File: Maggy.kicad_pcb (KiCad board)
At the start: 2 copper layers, 160 x 100 mm, 75 parts, among them CN1 0430450800, CN2 430451000, J1 XY308-2.54-2P, J2 XY308-2.54-2P, J3 XY308-2.54-2P, J4 XY308-2.54-2P, U1 CH224K, U10 INA214AIDCKR, U11 Socket for Teensy 4.1 (2x 1x2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, U12 INA214AIDCKR, U13 INA214AIDCKR, U14 TMAG5170A2DGKR, U15 TMAG5170A2DGKR, U16 TMAG5170A2DGKR, U17 TMAG5170A2DGKR, U18 TMAG5170A2DGKR, U2 A4950ELJTR-T, U3 A4950ELJTR-T, U4 A4950ELJTR-T, U5 A4950ELJTR-T, U6 TLV2372, U7 LM1117S-3.3, U8 LM1117S-5.0, U9 INA214AIDCKR

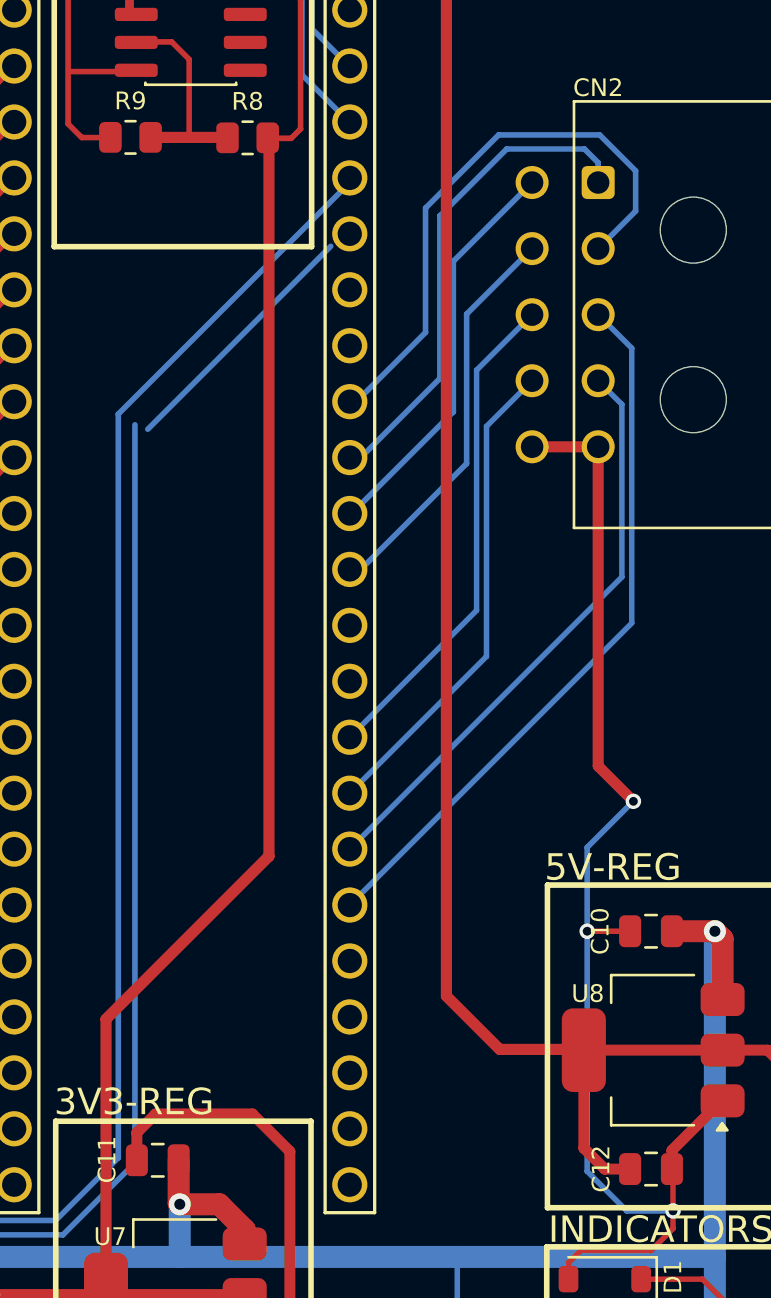
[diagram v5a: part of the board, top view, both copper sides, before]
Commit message: fix: disconnected CUR_SOL_3 trace
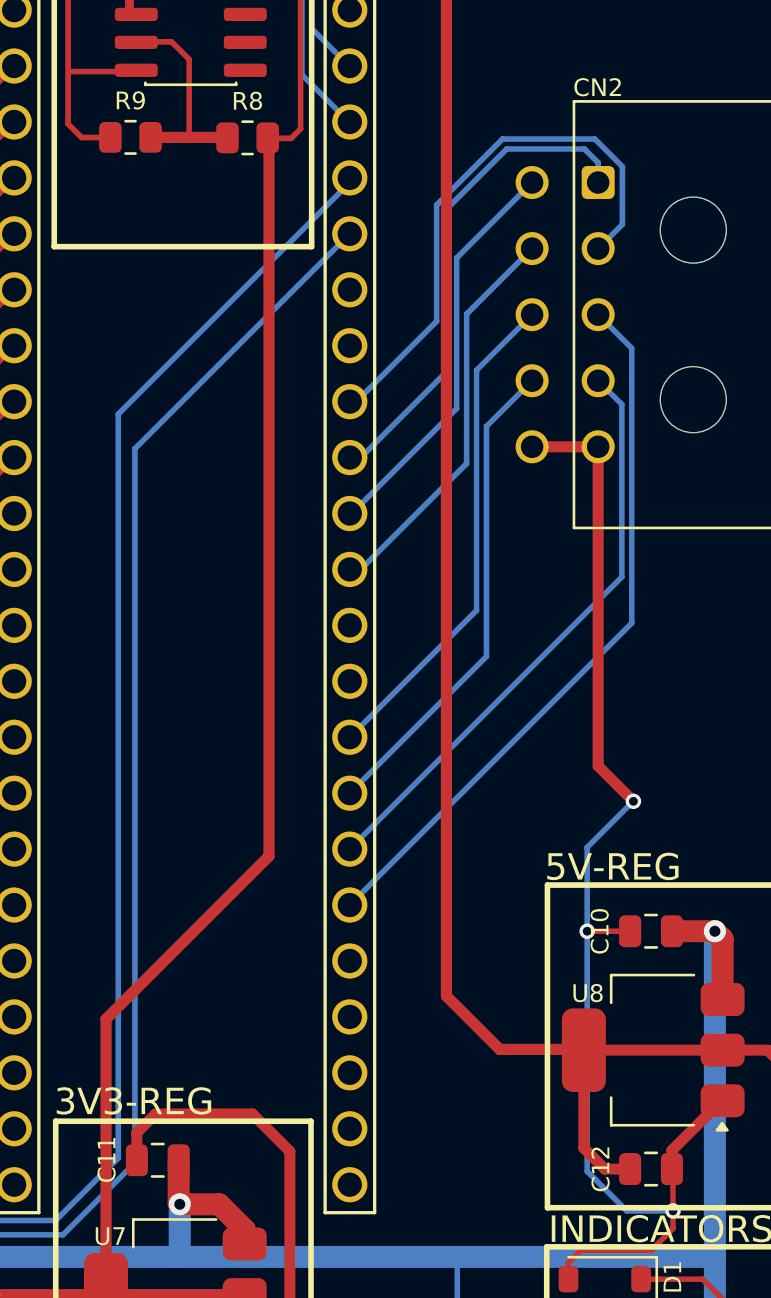
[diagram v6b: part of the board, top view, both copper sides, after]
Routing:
- net UX_P_OUT: track 26.2 -> 25.1 mm
- net CUR_SOL3: track 70.5 -> 71.5 mm
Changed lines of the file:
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@@
+	)
+	(segment
+		(start 186.34 121.8565)
+		(end 186.262 121.8565)
+		(width 0.254)
+		(layer "B.Cu")
+		(net "CUR_SOL3")
+	)
+	(segment
+		(start 199.663 87.687)
+		(end 199.663 120.118)
+		(width 0.254)
+		(layer "B.Cu")
+		(net "CUR_SOL3")
+	)
+	(segment
+		(start 209.42 77.93)
+		(end 199.663 87.687)
+		(width 0.254)
+		(layer "B.Cu")
+		(net "CUR_SOL3")
 	)
 	(segment
@@
 		(start 196.395 123.3865)
 		(end 187.87 123.3865)
-		(width 0.254)
-		(layer "B.Cu")
-		(net "CUR_SOL3")
-	)
-	(segment
-		(start 186.34 121.8565)
-		(end 186.262 121.8565)
-		(width 0.254)
-		(layer "B.Cu")
-		(net "CUR_SOL3")
-	)
-	(segment
-		(start 208.554 78.4965)
-		(end 200.2475 86.8025)
-		(width 0.254)
-		(layer "B.Cu")
-		(net "CUR_SOL3")
-	)
-	(segment
-		(start 199.663 86.601)
-		(end 199.663 120.118)
 		(width 0.254)
 		(layer "B.Cu")
@@
 	)
 	(segment
-		(start 214.1245 79.1755)
+		(start 214.272 79.028)
 		(end 217.7 75.6)
-		(width 0.254)
-		(layer "B.Cu")
-		(net "UY_P_OUT")
-	)
-	(segment
-		(start 214.1245 86.0115)
-		(end 214.1245 79.1755)
 		(width 0.254)
 		(layer "B.Cu")
@@
 	)
 	(segment
+		(start 214.272 85.8635)
+		(end 214.272 79.028)
+		(width 0.254)
+		(layer "B.Cu")
+		(net "UY_P_OUT")
+	)
+	(segment
 		(start 209.472 90.6635)
-		(end 214.1245 86.0115)
+		(end 214.272 85.8635)
 		(width 0.254)
 		(layer "B.Cu")
 		(net "UY_P_OUT")
+	)
+	(segment
+		(start 213.818 76.806)
+		(end 216.5465 74.0775)
+		(width 0.254)
+		(layer "B.Cu")
+		(net "UX_N_OUT")
+	)
+	(segment
+		(start 216.5465 74.0775)
+		(end 220.0775 74.0775)
+		(width 0.254)
+		(layer "B.Cu")
+		(net "UX_N_OUT")
+	)
+	(segment
+		(start 220.0775 74.0775)
+		(end 220.7 74.7)
+		(width 0.254)
+		(layer "B.Cu")
+		(net "UX_N_OUT")
+	)
+	(segment
+		(start 209.5305 88.118)
+		(end 209.89 88.118)
+		(width 0.254)
+		(layer "B.Cu")
+		(net "UX_N_OUT")
 	)
 	(segment
@@
 	)
 	(segment
-		(start 209.5305 88.118)
-		(end 209.89 88.118)
+		(start 209.89 88.118)
+		(end 213.818 84.19)
 		(width 0.254)
 		(layer "B.Cu")
@@
 	)
 	(segment
-		(start 216.5465 74.0775)
-		(end 220.0775 74.0775)
-		(width 0.254)
-		(layer "B.Cu")
-		(net "UX_N_OUT")
-	)
-	(segment
-		(start 213.511 77.113)
-		(end 216.5465 74.0775)
-		(width 0.254)
-		(layer "B.Cu")
-		(net "UX_N_OUT")
-	)
-	(segment
-		(start 213.511 84.4965)
-		(end 213.511 77.113)
-		(width 0.254)
-		(layer "B.Cu")
-		(net "UX_N_OUT")
-	)
-	(segment
-		(start 209.89 88.118)
-		(end 213.511 84.4965)
+		(start 213.818 84.19)
+		(end 213.818 76.806)
 		(width 0.254)
 		(layer "B.Cu")
@@
 	)
 	(segment
-		(start 220.0775 74.0775)
-		(end 220.7 74.7)
-		(width 0.254)
-		(layer "B.Cu")
-		(net "UX_N_OUT")
-	)
-	(segment
-		(start 212.8615 82.407)
-		(end 212.8615 76.7565)
+		(start 213.364 81.904)
+		(end 213.364 76.617947)
 		(width 0.254)
 		(layer "B.Cu")
@@
 	)
 	(segment
-		(start 209.705 85.563)
-		(end 212.8615 82.407)
+		(start 220.546428 73.6235)
+		(end 221.8 74.877072)
+		(width 0.254)
+		(layer "B.Cu")
+		(net "UX_P_OUT")
+	)
+	(segment
+		(start 213.364 76.617947)
+		(end 216.358448 73.6235)
+		(width 0.254)
+		(layer "B.Cu")
+		(net "UX_P_OUT")
+	)
+	(segment
+		(start 209.5455 85.563)
+		(end 209.705 85.563)
+		(width 0.254)
+		(layer "B.Cu")
+		(net "UX_P_OUT")
+	)
+	(segment
+		(start 216.358448 73.6235)
+		(end 220.546428 73.6235)
 		(width 0.254)
 		(layer "B.Cu")
@@
 	)
 	(segment
-		(start 212.8615 76.7565)
-		(end 216.1795 73.438)
+		(start 221.8 77.5)
+		(end 220.7 78.6)
 		(width 0.254)
 		(layer "B.Cu")
@@
 	)
 	(segment
-		(start 220.7695 73.438)
-		(end 222.4 75.0685)
+		(start 209.705 85.563)
+		(end 213.364 81.904)
 		(width 0.254)
 		(layer "B.Cu")
@@
 	)
 	(segment
-		(start 209.5455 85.563)
-		(end 209.705 85.563)
-		(width 0.254)
-		(layer "B.Cu")
-		(net "UX_P_OUT")
-	)
-	(segment
-		(start 222.4 76.9)
-		(end 220.7 78.6)
-		(width 0.254)
-		(layer "B.Cu")
-		(net "UX_P_OUT")
-	)
-	(segment
-		(start 216.1795 73.438)
-		(end 220.7695 73.438)
-		(width 0.254)
-		(layer "B.Cu")
-		(net "UX_P_OUT")
-	)
-	(segment
-		(start 222.4 75.0685)
-		(end 222.4 76.9)
-		(width 0.254)
-		(layer "B.Cu")
+		(start 221.8 74.877072)
+		(end 221.8 77.5)
+		(width 0.254)
+		(layer "B.Cu")
